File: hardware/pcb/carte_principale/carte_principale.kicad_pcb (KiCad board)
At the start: 2 copper layers, 54.5 x 50 mm, 25 parts, among them J1 Arduino_UNO_R3, J2 Conn_01x02, J3 Conn_01x02, P1 TE-FFC-10-0.5, P2 TE-FFC-10-0.5, U1 ESP-WROOM-02, U2 LSM6DS3, U3 BMP280, U5 74AHC1G125, U6 74LS166, U7 LIS2MDL

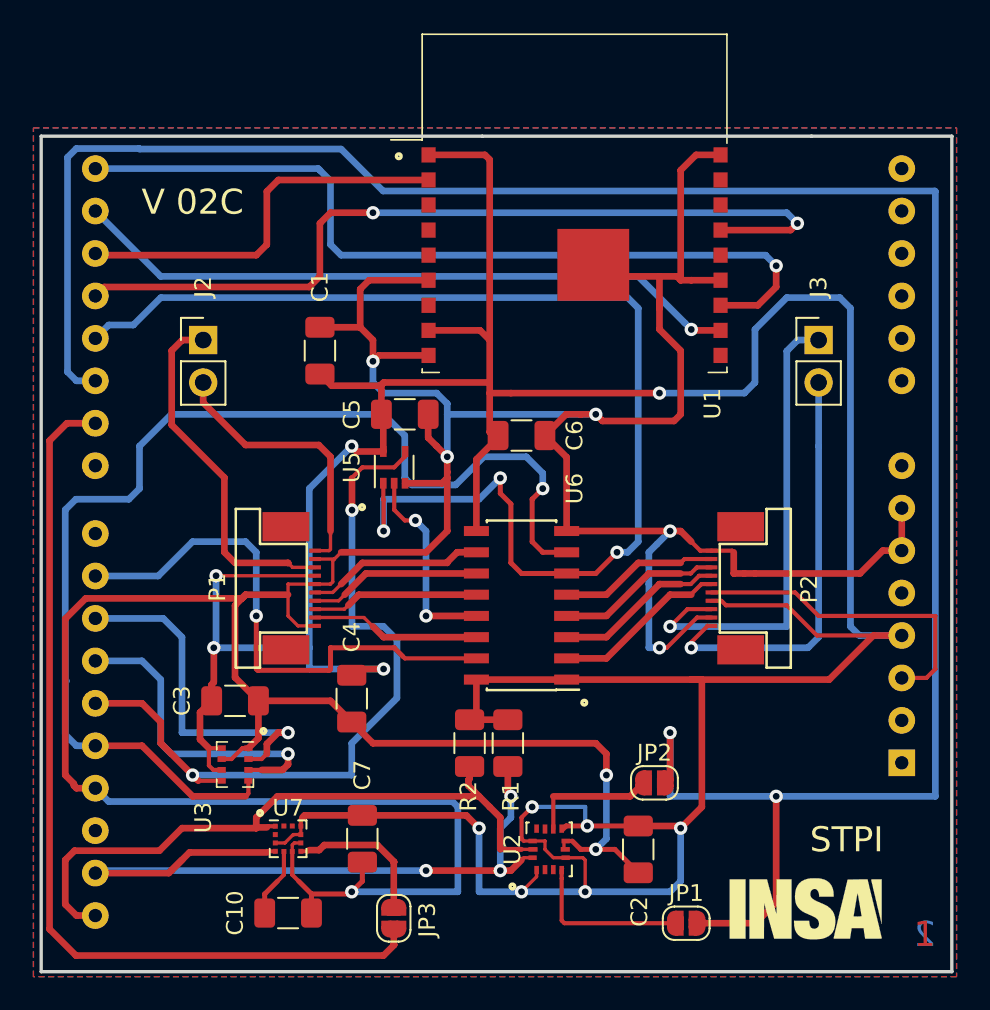
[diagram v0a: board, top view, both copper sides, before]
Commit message: Refresh de la carte capteur
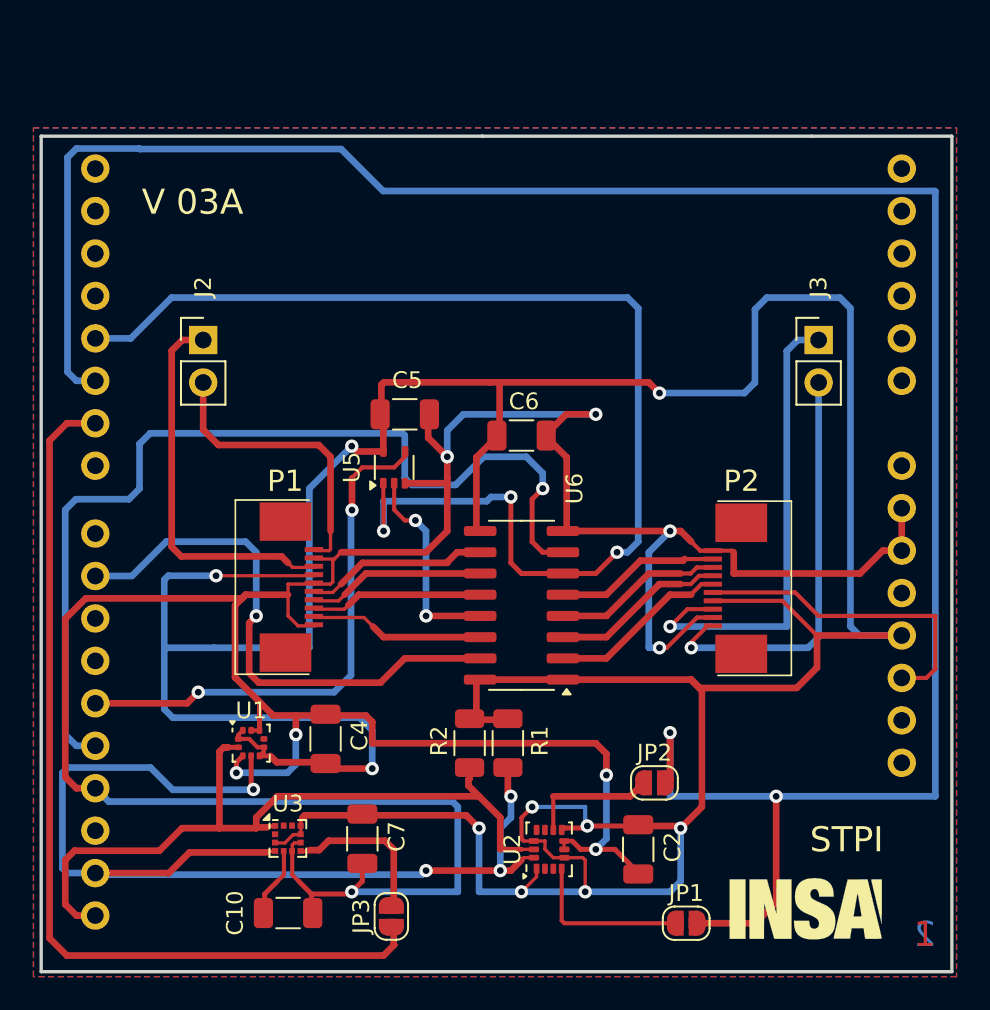
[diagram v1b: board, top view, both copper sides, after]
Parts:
- removed C1, C3: 100nF, Capacitor_SMD:C_1206_3216Metric
- removed U7: LIS2MDL, Insa:LGA-12_2x2mm_P0.5mm-slim
- P1, P2: value TE-FFC-10-0.5 -> 1-1734592-0; footprint Insa:FFC-10-0.5 -> 1-1734592-0:117345920
- U1: value ESP-WROOM-02 -> LPS22DF; footprint RF_Module:ESP-WROOM-02 -> Package_LGA:ST_HLGA-10_2x2mm_P0.5mm_LayoutBorder3x2y
- U2: footprint Insa:LGA-14_3x2.5mm_P0.5mm_LayoutBorder3x4y-slim -> Package_LGA:LGA-14_3x2.5mm_P0.5mm_LayoutBorder3x4y
- U3: value BMP280 -> LIS2MDL; footprint Package_LGA:Bosch_LGA-8_2x2.5mm_P0.65mm_ClockwisePinNumbering -> Package_LGA:LGA-12_2x2mm_P0.5mm
- U6: value 74LS166 -> 74HC166
- moved U1 35.0 mm to (102.6, 100.3)
- moved U3 5.44 mm to (104.8, 106.0), turned to 0 degrees
- moved C4 2.87 mm to (107.0, 100.1), turned to 90 degrees
- moved P2 2.08 mm to (132.5, 91.1), turned to 90 degrees
- moved P1 2.08 mm to (104.0, 91.0), turned to -90 degrees
- moved JP3 0.18 mm to (111.0, 110.7)
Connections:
- C10 pad 1: Net-(C10-Pad1) -> Net-(U3-C1)
- J1 pad 1: Net-(J1-Pad1) -> unconnected-(J1-NC-Pad1)
- J1 pad 10: Net-(J1-Pad10) -> unconnected-(J1-A1-Pad10)
- J1 pad 11: Net-(J1-Pad11) -> unconnected-(J1-A2-Pad11)
- J1 pad 12: Net-(J1-Pad12) -> unconnected-(J1-A3-Pad12)
- J1 pad 13: Net-(J1-Pad13) -> unconnected-(J1-A4/SDA-Pad13)
- J1 pad 14: Net-(J1-Pad14) -> unconnected-(J1-A5/SCL-Pad14)
- J1 pad 15: /WIFI_TX -> unconnected-(J1-D0/RX-Pad15)
- J1 pad 16: /WIFI_RX -> unconnected-(J1-D1/TX-Pad16)
- J1 pad 17: /WIFI_EN -> unconnected-(J1-D2-Pad17)
- J1 pad 18: /WIFI_RST -> unconnected-(J1-D3-Pad18)
- J1 pad 2: Net-(J1-Pad2) -> unconnected-(J1-IOREF-Pad2)
- J1 pad 22: Net-(J1-Pad22) -> unconnected-(J1-D7-Pad22)
- J1 pad 23: Net-(J1-Pad23) -> unconnected-(J1-D8-Pad23)
- J1 pad 25: /BMP280_EN -> unconnected-(J1-D10-Pad25)
- J1 pad 26: /SPI_MOSI -> unconnected-(J1-D11-Pad26)
- J1 pad 30: Net-(J1-Pad30) -> unconnected-(J1-AREF-Pad30)
- J1 pad 5: Net-(J1-Pad5) -> unconnected-(J1-+5V-Pad5)
- J1 pad 8: Net-(J1-Pad8) -> unconnected-(J1-VIN-Pad8)
- J1 pad 9: Net-(J1-Pad9) -> unconnected-(J1-A0-Pad9)
- JP3 pad 2: Net-(JP3-Pad2) -> Net-(JP3-B)
- P1 pad 1: GND -> /Audio_Left_1
- P1 pad 10: /Audio_Left_1 -> GND
- P1 pad 2: /Key_Down -> GND
- P1 pad 3: /Key_Up -> /Audio_Left_2
- P1 pad 4: /Key_Right -> VCC
- P1 pad 5: /Key_Left -> GND
- P1 pad 6: GND -> /Key_Left
- P1 pad 7: VCC -> /Key_Right
- P1 pad 8: /Audio_Left_2 -> /Key_Up
- P1 pad 9: GND -> /Key_Down
- P2 pad 1: GND -> /Audio_Right_1
- P2 pad 10: /Audio_Right_1 -> GND
- P2 pad 2: /Key_X -> GND
- P2 pad 3: /Key_Y -> /Audio_Right_2
- P2 pad 4: /Key_A -> VCC
- P2 pad 5: /Key_B -> /KEY_RST
- P2 pad 6: /KEY_RST -> /Key_B
- P2 pad 7: VCC -> /Key_A
- P2 pad 8: /Audio_Right_2 -> /Key_Y
- P2 pad 9: GND -> /Key_X
- U1 pad 10: Net-(U1-Pad10) -> VCC
- U1 pad 2: /WIFI_EN -> /I2C_SCL
- U1 pad 3: Net-(U1-Pad3) -> GND
- U1 pad 4: Net-(U1-Pad4) -> /I2C_SDA
- U1 pad 5: Net-(U1-Pad5) -> VCC
- U1 pad 6: GND -> VCC
- U1 pad 7: Net-(U1-Pad7) -> unconnected-(U1-INT_DRDY-Pad7)
- U1 pad 8: VCC -> GND
- U2 pad 10: Net-(U2-Pad10) -> unconnected-(U2-NC-Pad10)
- U2 pad 11: Net-(U2-Pad11) -> unconnected-(U2-NC-Pad11)
- U2 pad 2: Net-(U2-Pad2) -> unconnected-(U2-SDX-Pad2)
- U2 pad 3: Net-(U2-Pad3) -> unconnected-(U2-SCX-Pad3)
- U3 pad 1: GND -> /I2C_SCL
- U3 pad 2: /BMP280_EN -> unconnected-(U3-NC-Pad2)
- U3 pad 3: /SPI_MOSI -> VCC
- U3 pad 4: /SPI_SCK -> /I2C_SDA
- U3 pad 5: /SPI_MISO -> Net-(U3-C1)
- U3 pad 6: VCC -> GND
- U3 pad 7: GND -> Net-(JP3-B)
- U3 pad 8: VCC -> GND
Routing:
- net /WIFI_RST: track 51.0 -> 0.00 mm, vias 2 -> 0
- net /WIFI_TX: track 50.4 -> 0.00 mm, vias 1 -> 0
- net GND: track 254.0 -> 204.8 mm, vias 8 -> 9
- net /WIFI_RX: track 40.4 -> 0.00 mm, vias 1 -> 0
- net /WIFI_EN: track 23.7 -> 0.00 mm
- net /I2C_SDA: track 45.5 -> 66.6 mm, vias 3 -> 4
- net /BMP280_EN: track 21.1 -> 0.00 mm, vias 1 -> 0
- net /SPI_MOSI: track 19.2 -> 0.00 mm, vias 1 -> 0
- net /SPI_MISO: track 44.9 -> 31.8 mm
- net /SPI_SCK: track 70.3 -> 57.7 mm
- net Net-(JP3-B): track 0.00 -> 9.50 mm
- net Net-(JP3-Pad2): track 8.89 -> 0.00 mm
- net VCC: track 248.9 -> 240.3 mm, vias 11 -> 10
- net /I2C_SCL: track 40.4 -> 46.3 mm
- net Net-(U3-C1): track 0.00 -> 4.16 mm
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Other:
- net class Default removed
- net class Insa_GEI removed
- net class Power removed
- rule pad_to_mask_clearance: 0.051 -> 0
- board text added: "V 03A"
- board text removed: "V 02C"
